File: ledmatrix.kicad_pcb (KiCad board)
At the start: 2 copper layers, 75.6 x 37.8 mm, 27 parts, among them J1 BUS_IN1, J2 BUS_IN2, J3 BUS_OUT1, J4 BUS_OUT2, Q1 PMV50XP, Q2 PMV50XP, Q3 PMV50XP, Q4 PMV50XP, Q5 PMV50XP, Q6 PMV50XP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

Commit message: fix matrix module order
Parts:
- Q7, R9: moved to B.Cu
- moved Q7 45.1 mm to (37.9, 38.4), turned to 180 degrees
- moved R9 44.9 mm to (38.4, 35.6), turned to 180 degrees
- moved U1 37.8 mm to (82.1, 44.3)
- moved U3 37.8 mm to (44.3, 44.3)
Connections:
- U2 pad 13: /matrix_1/COL_EN -> /GND
- U4 pad 13: /matrix_1/COL_EN -> /GND
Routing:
- net /CDO: track 0.00 -> 100.0 mm
- net /matrix_2/COL_DI: track 0.00 -> 40.3 mm, vias 0 -> 4
- net Net-(U3-Pad3): track 22.4 -> 0.00 mm, vias 1 -> 0
- net Net-(U3-Pad4): track 22.2 -> 0.00 mm, vias 1 -> 0
- net /Row Control/RC7: track 0.00 -> 21.9 mm, vias 0 -> 1
- net /CLE: track 61.6 -> 83.1 mm
- net Net-(U3-Pad11): track 16.5 -> 0.00 mm, vias 1 -> 0
- net Net-(U3-Pad6): track 11.9 -> 0.00 mm
- net /ROW_7: track 38.8 -> 41.1 mm
- net Net-(Q7-Pad1): track 0.00 -> 1.92 mm

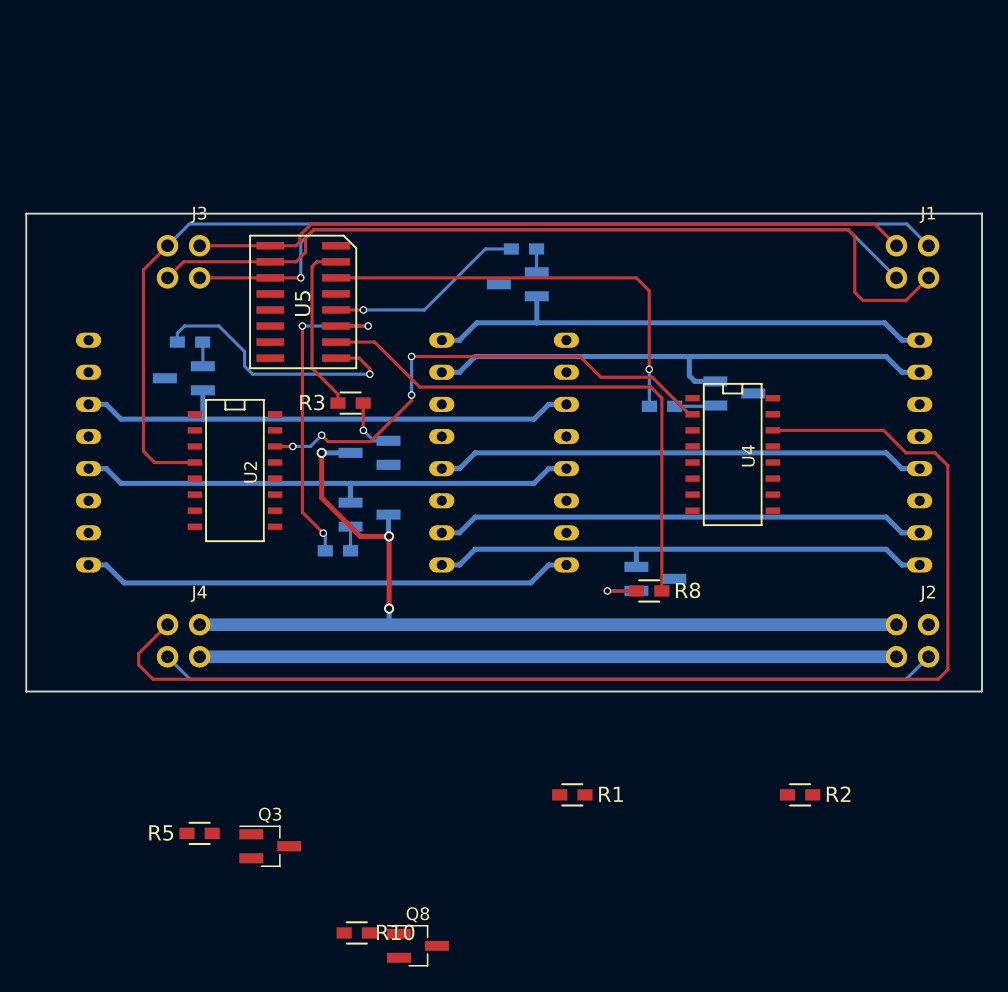
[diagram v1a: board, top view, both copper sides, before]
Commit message: cleaner vcc, gnd on left side
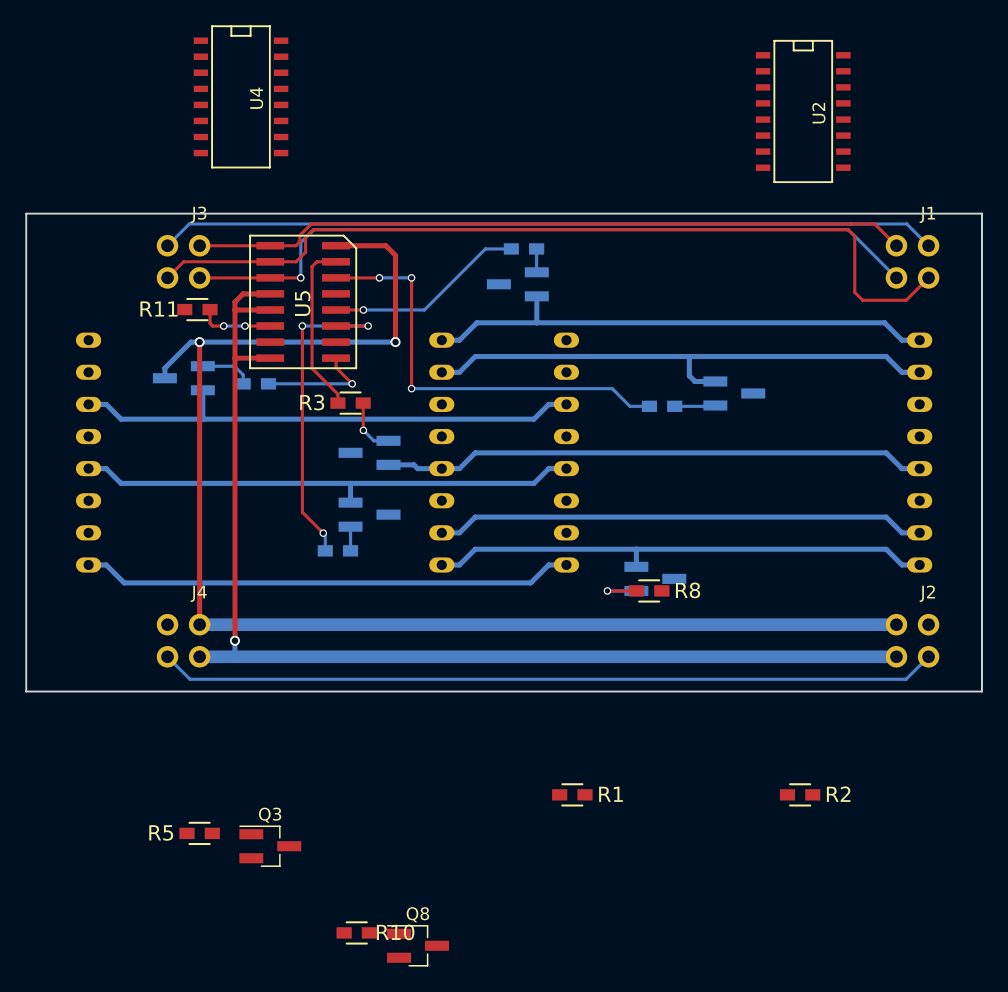
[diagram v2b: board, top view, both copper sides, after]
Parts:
- added R11: 10k, footprints:0603_HAND, F.Cu at (38.9, 33.0)
- moved U2 53.2 mm to (86.9, 17.3)
- moved U4 48.1 mm to (42.4, 16.2)
- moved R9 6.17 mm to (43.6, 38.9), turned to 0 degrees
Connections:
- U5 pad 6: (no net) -> /REN
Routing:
- net /CDO: track 100.0 -> 0.00 mm
- net /Row Control/RC6: track 42.9 -> 0.00 mm
- net /matrix_2/COL_DI: track 40.3 -> 0.00 mm, vias 4 -> 0
- net /GND: track 55.1 -> 91.8 mm, vias 0 -> 1
- net /VCC: track 76.3 -> 109.2 mm, vias 3 -> 2
- net /CLE: track 83.1 -> 61.6 mm
- net /Row Control/RC7: track 21.9 -> 9.18 mm
- net /REN: track 0.00 -> 5.95 mm, vias 0 -> 2
- net /ROW_1: track 39.7 -> 44.0 mm
- net Net-(Q7-Pad1): track 1.92 -> 4.18 mm
- net /Row Control/RC2: track 34.3 -> 34.1 mm, vias 1 -> 3

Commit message: finish left side traces
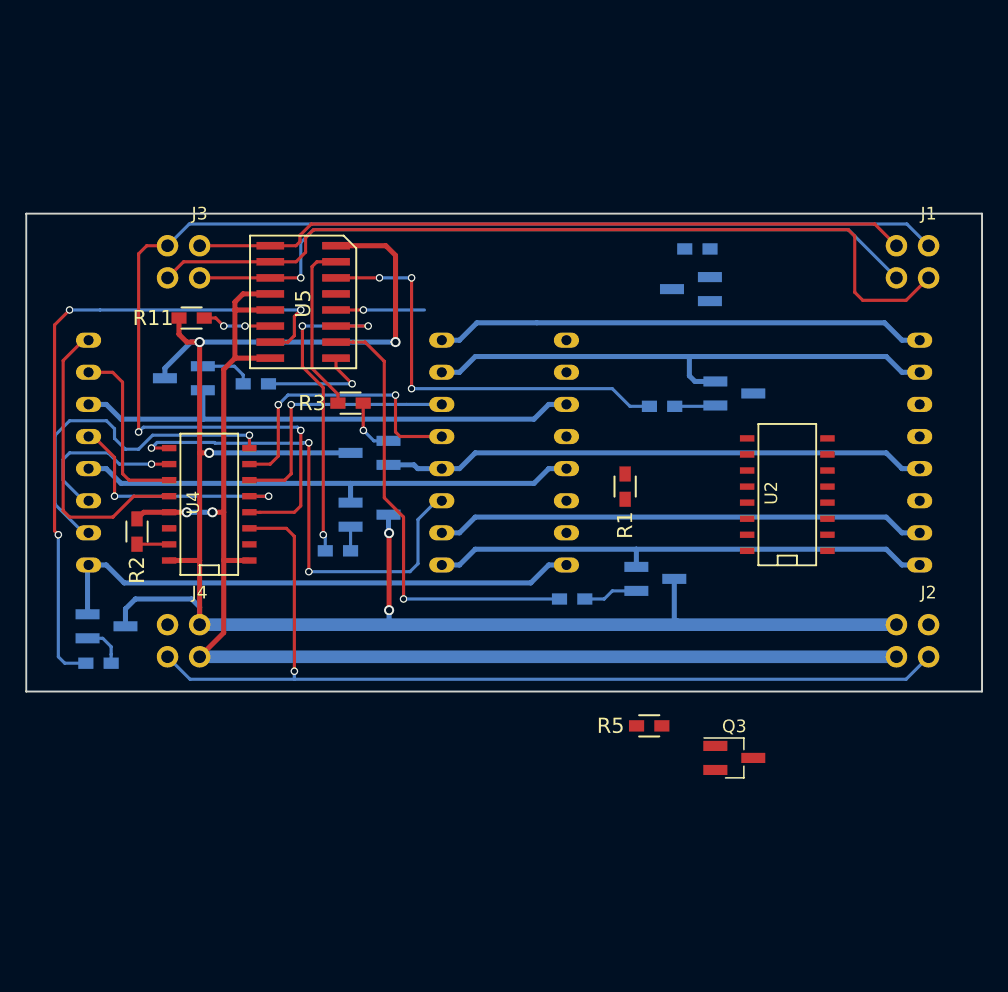
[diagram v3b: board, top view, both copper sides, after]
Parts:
- Q8, R10, R8: moved to B.Cu
- moved R2 56.4 mm to (34.2, 50.5), turned to 270 degrees
- moved Q3 37.4 mm to (81.4, 68.5)
- moved R5 36.6 mm to (74.7, 65.9)
- moved Q8 35.3 mm to (31.8, 58.0)
- moved U4 32.3 mm to (39.9, 48.4), turned to 90 degrees
- moved U2 30.3 mm to (85.6, 47.6), turned to 90 degrees
- moved R10 29.5 mm to (31.1, 61.0), turned to 180 degrees
- moved R1 24.7 mm to (72.8, 47.0), turned to 270 degrees
- moved R6 13.7 mm to (78.5, 28.2)
- moved Q4 13.7 mm to (78.0, 31.4)
- moved R8 6.13 mm to (68.6, 55.9), turned to 180 degrees
- moved R11 0.81 mm to (38.5, 33.7)
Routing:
- net /Row Control/RC8: track 0.00 -> 53.1 mm, vias 0 -> 3
- net /CLE: track 61.6 -> 101.6 mm, vias 0 -> 2
- net Net-(U3-Pad6): track 0.00 -> 39.9 mm, vias 0 -> 3
- net /VCC: track 109.2 -> 148.4 mm, vias 2 -> 5
- net /Row Control/RC6: track 0.00 -> 36.2 mm, vias 0 -> 1
- net Net-(U3-Pad10): track 0.00 -> 28.2 mm, vias 0 -> 1
- net Net-(U3-Pad16): track 0.00 -> 23.8 mm
- net Net-(U3-Pad4): track 0.00 -> 23.3 mm, vias 0 -> 2
- net Net-(U3-Pad3): track 0.00 -> 21.2 mm, vias 0 -> 1
- net Net-(U3-Pad13): track 0.00 -> 20.2 mm, vias 0 -> 2
- net /CCK: track 61.7 -> 76.8 mm, vias 0 -> 1
- net Net-(U3-Pad15): track 0.00 -> 14.5 mm
- net Net-(U3-Pad11): track 0.00 -> 13.4 mm, vias 0 -> 1
- net /GND: track 91.8 -> 102.1 mm, vias 1 -> 2
- net /Row Control/RC4: track 15.9 -> 6.99 mm
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
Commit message: add bypassing to schematic
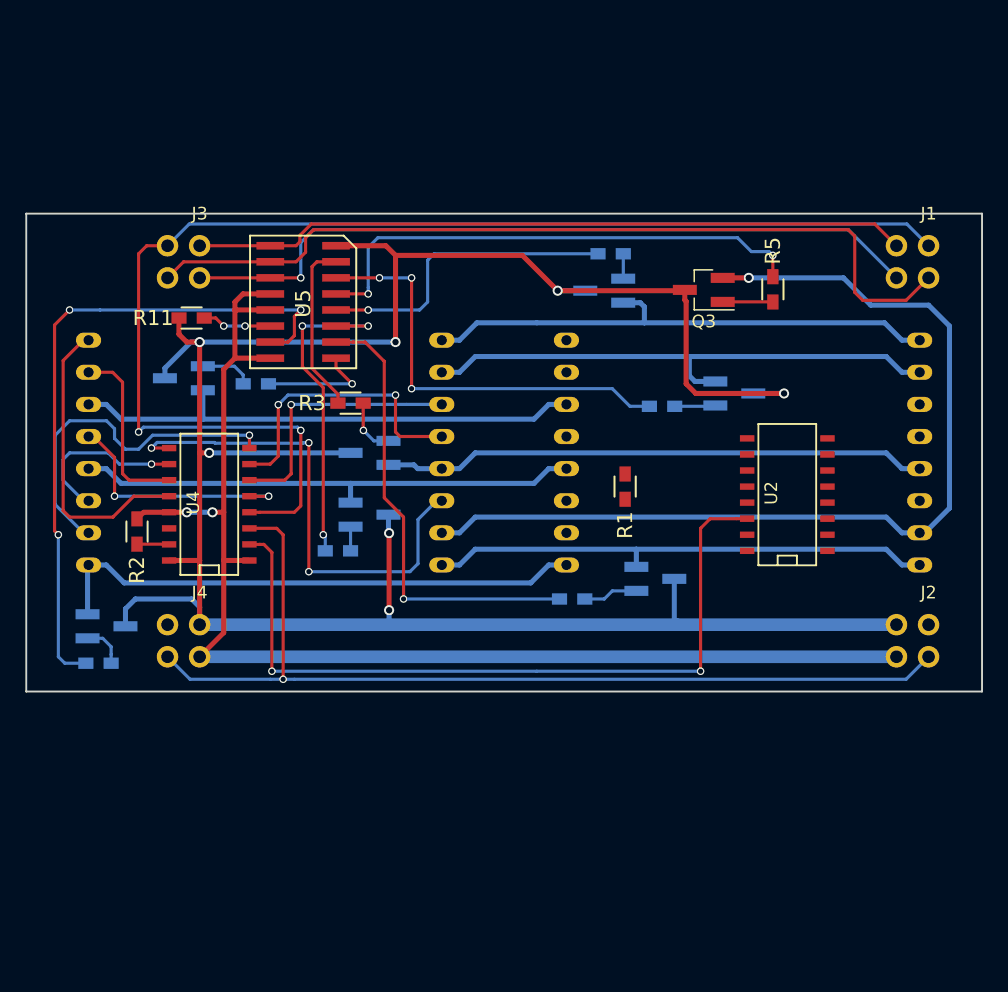
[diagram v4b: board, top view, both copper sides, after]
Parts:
- moved Q3 37.1 mm to (79.0, 31.4), turned to 180 degrees
- moved R5 35.9 mm to (84.5, 31.4), turned to 90 degrees
- moved R6 6.87 mm to (71.6, 28.6)
- moved Q4 6.86 mm to (71.1, 31.5)
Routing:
- net /matrix_2/COL_DI: track 0.00 -> 60.6 mm, vias 0 -> 2
- net /VCC: track 148.4 -> 192.6 mm, vias 5 -> 7
- net /Row Control/RC3: track 0.00 -> 40.8 mm, vias 0 -> 2
- net /ROW_3: track 38.8 -> 75.9 mm, vias 0 -> 1
- net /Row Control/RC4: track 6.99 -> 24.5 mm
- net Net-(Q3-Pad1): track 0.00 -> 3.96 mm
- net /ROW_4: track 39.3 -> 42.4 mm
- net Net-(Q4-Pad1): track 0.00 -> 1.97 mm

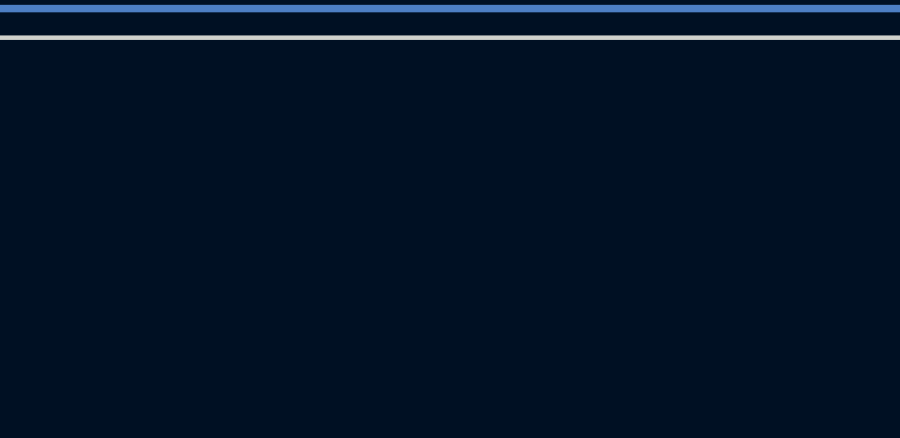
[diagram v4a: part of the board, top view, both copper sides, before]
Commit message: read bypassing netlist into pcbnew
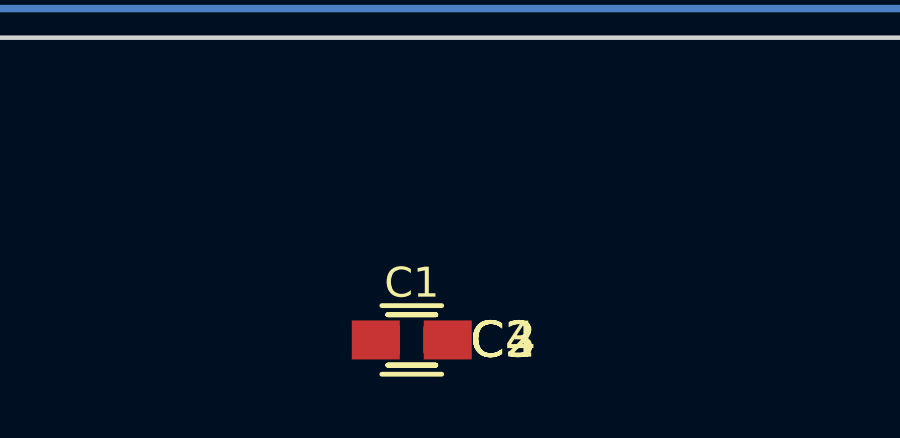
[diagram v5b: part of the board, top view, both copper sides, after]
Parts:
- added C1: 10u, footprints:0805_HAND, F.Cu at (63.2, 73.3)
- added C2, C3, C4: 1u, footprints:0603_HAND, F.Cu at (63.2, 73.3)
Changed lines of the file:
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@@
 (kicad_pcb (version 4) (host pcbnew 4.0.6)
   (general
-    (links 89)
-    (no_connects 27)
-    (area 25.024999 24.325 106.999001 72.128)
+    (links 96)
+    (no_connects 21)
+    (area 25.324999 25.324999 101.075001 63.275001)
     (thickness 1.6)
     (drawings 4)
     (tracks 394)
     (zones 0)
-    (modules 28)
+    (modules 32)
     (nets 54)
   )
@@
       (net 1 /VCC))
   )
+  (module footprints:0805_HAND (layer F.Cu)
+    (at 63.2 73.275001)
+    (fp_text reference C1 (at 0 -1.905) (layer F.SilkS)
+      (effects (font (size 1 1) (thickness 0.16)))
+    )
+    (fp_text value 10u (at 0 2.032) (layer F.Fab)
+      (effects (font (size 1 1) (thickness 0.16)))
+    )
+    (fp_line (start -1 1.143) (end 1 1.143) (layer F.SilkS) (width 0.16))
+    (fp_line (start -1 -1.143) (end 1 -1.143) (layer F.SilkS) (width 0.16))
+    (pad 1 smd rect (at -1.2 0) (size 1.6 1.3) (layers F.Cu F.Paste F.Mask))
+    (pad 2 smd rect (at 1.2 0) (size 1.6 1.3) (layers F.Cu F.Paste F.Mask)
+      (net 2 /GND))
+  )
+  (module footprints:0603_HAND (layer F.Cu)
+    (at 63.2 73.275001)
+    (fp_text reference C2 (at 3.048 0) (layer F.SilkS)
+      (effects (font (size 1.2 1.2) (thickness 0.2)))
+    )
+    (fp_text value 1u (at 0 1.651) (layer F.Fab)
+      (effects (font (size 1.2 1.2) (thickness 0.2)))
+    )
+    (fp_line (start -0.8 0.84) (end 0.8 0.84) (layer F.SilkS) (width 0.16))
+    (fp_line (start -0.8 -0.84) (end 0.8 -0.84) (layer F.SilkS) (width 0.16))
+    (pad 1 smd rect (at -1 0) (size 1.2 0.9) (layers F.Cu F.Paste F.Mask)
+      (net 1 /VCC))
+    (pad 2 smd rect (at 1 0) (size 1.2 0.9) (layers F.Cu F.Paste F.Mask)
+      (net 2 /GND))
+  )
+  (module footprints:0603_HAND (layer F.Cu)
+    (at 63.2 73.275001)
+    (fp_text reference C3 (at 3.048 0) (layer F.SilkS)
+      (effects (font (size 1.2 1.2) (thickness 0.2)))
+    )
+    (fp_text value 1u (at 0 1.651) (layer F.Fab)
+      (effects (font (size 1.2 1.2) (thickness 0.2)))
+    )
+    (fp_line (start -0.8 0.84) (end 0.8 0.84) (layer F.SilkS) (width 0.16))
+    (fp_line (start -0.8 -0.84) (end 0.8 -0.84) (layer F.SilkS) (width 0.16))
+    (pad 1 smd rect (at -1 0) (size 1.2 0.9) (layers F.Cu F.Paste F.Mask)
+      (net 1 /VCC))
+    (pad 2 smd rect (at 1 0) (size 1.2 0.9) (layers F.Cu F.Paste F.Mask)
+      (net 2 /GND))
+  )
+  (module footprints:0603_HAND (layer F.Cu)
+    (at 63.2 73.275001)
+    (fp_text reference C4 (at 3.048 0) (layer F.SilkS)
+      (effects (font (size 1.2 1.2) (thickness 0.2)))
+    )
+    (fp_text value 1u (at 0 1.651) (layer F.Fab)
+      (effects (font (size 1.2 1.2) (thickness 0.2)))
+    )
+    (fp_line (start -0.8 0.84) (end 0.8 0.84) (layer F.SilkS) (width 0.16))
+    (fp_line (start -0.8 -0.84) (end 0.8 -0.84) (layer F.SilkS) (width 0.16))
+    (pad 1 smd rect (at -1 0) (size 1.2 0.9) (layers F.Cu F.Paste F.Mask)
+      (net 2 /GND))
+    (pad 2 smd rect (at 1 0) (size 1.2 0.9) (layers F.Cu F.Paste F.Mask)
+      (net 1 /VCC))
+  )

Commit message: fully connected PCB
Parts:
- C1: moved to B.Cu
- moved C4 46.1 mm to (54.7, 27.9), turned to 180 degrees
- moved C3 29.7 mm to (40.0, 54.7)
- moved C2 29.3 mm to (85.6, 54.4)
- moved C1 24.7 mm to (42.9, 59.2), turned to 270 degrees
- moved R1 8.80 mm to (80.1, 51.8), turned to 90 degrees
- moved R9 0.72 mm to (43.1, 39.4)
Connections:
- C1 pad 1: (no net) -> /VCC
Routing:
- net /GND: track 102.1 -> 189.6 mm, vias 2 -> 7
- net /CLE: track 101.6 -> 133.3 mm
- net Net-(U1-Pad13): track 0.00 -> 31.6 mm, vias 0 -> 1
- net Net-(U1-Pad10): track 0.00 -> 28.4 mm, vias 0 -> 2
- net Net-(U1-Pad16): track 0.00 -> 23.3 mm
- net Net-(U1-Pad15): track 0.00 -> 22.3 mm, vias 0 -> 2
- net /CCK: track 76.3 -> 97.2 mm
- net /VCC: track 192.6 -> 210.4 mm, vias 7 -> 11
- net Net-(U1-Pad6): track 0.00 -> 17.6 mm, vias 0 -> 1
- net /CDO: track 0.00 -> 17.4 mm, vias 0 -> 2
- net Net-(U1-Pad11): track 0.00 -> 17.0 mm, vias 0 -> 1
- net /CDI: track 0.00 -> 14.3 mm
- net Net-(U1-Pad4): track 0.00 -> 12.6 mm, vias 0 -> 1
- net Net-(U1-Pad3): track 0.00 -> 11.9 mm
- net /Row Control/RC8: track 53.1 -> 48.2 mm
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
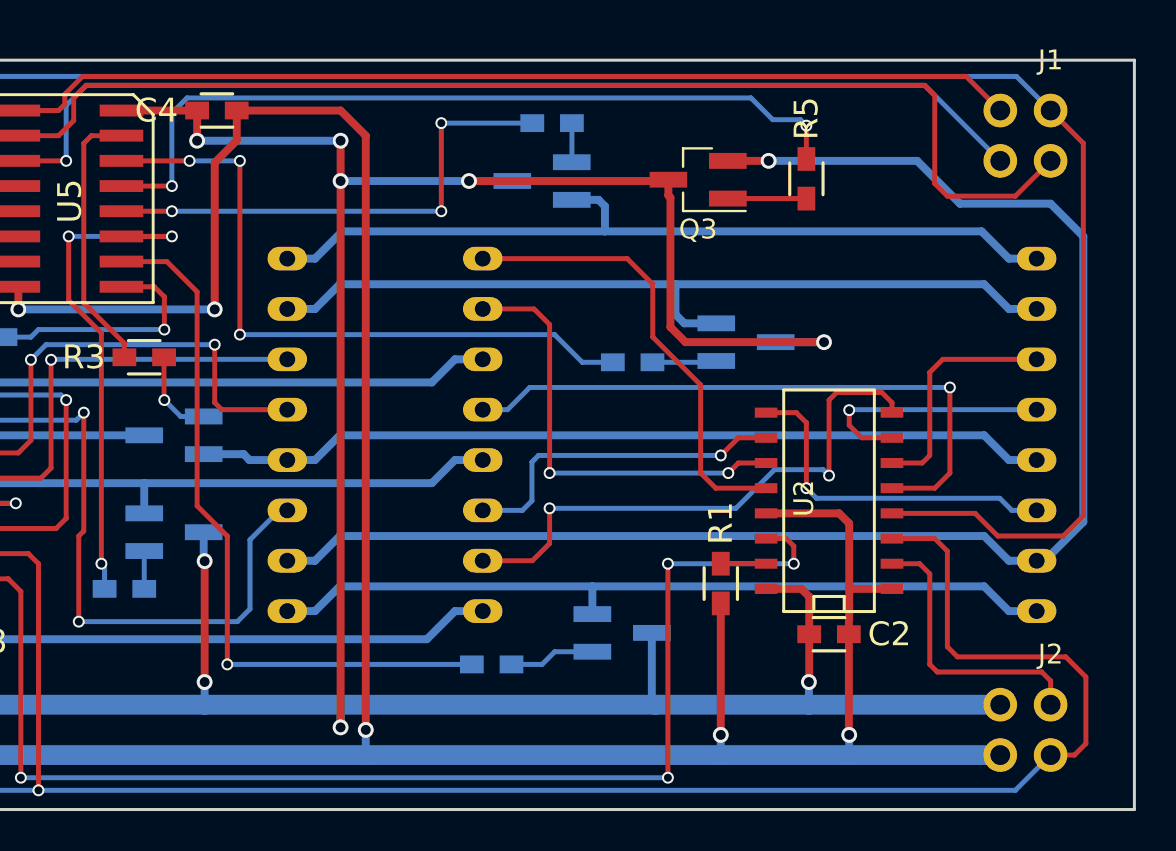
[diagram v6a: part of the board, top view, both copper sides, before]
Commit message: move R3 driver closer to R3
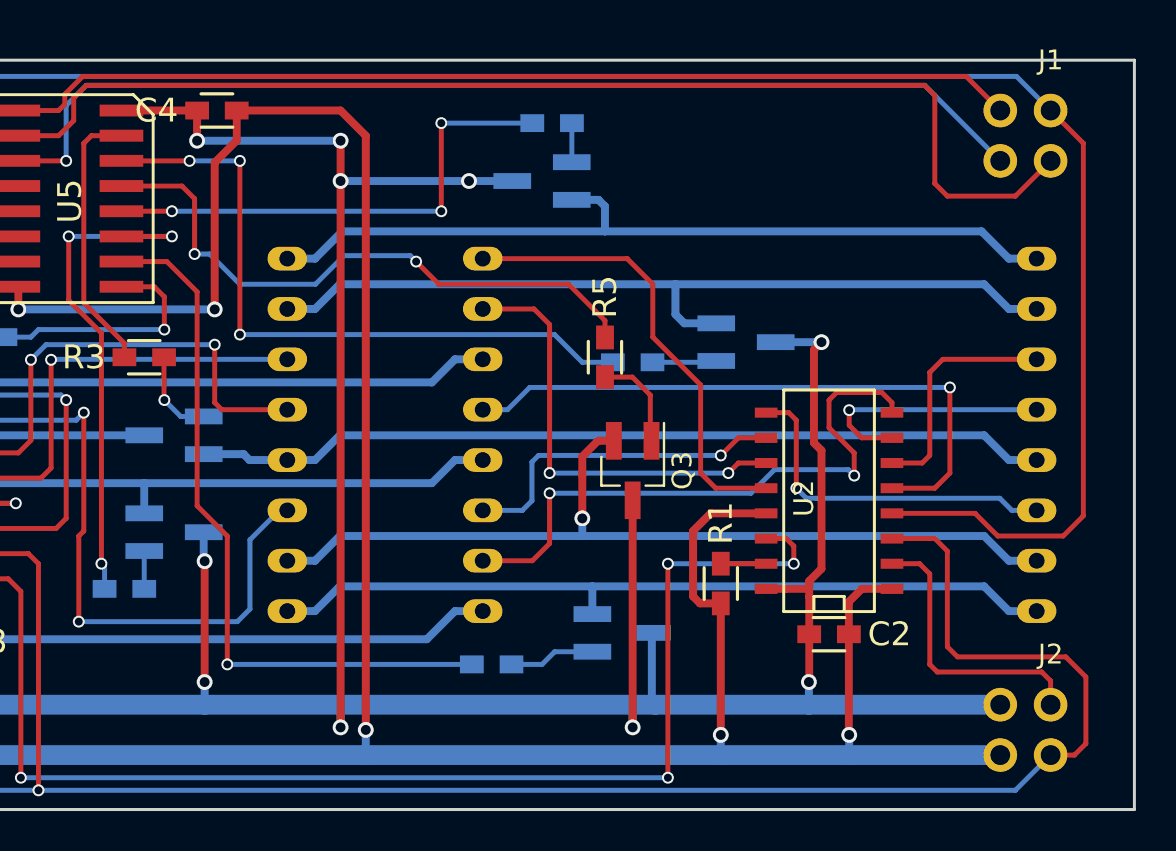
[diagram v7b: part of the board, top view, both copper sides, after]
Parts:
- moved Q3 15.0 mm to (75.7, 46.1), turned to 270 degrees
- moved R5 13.6 mm to (74.3, 40.4)
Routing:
- net /ROW_3: track 75.9 -> 45.2 mm
- net /Row Control/RC3: track 40.8 -> 30.9 mm
- net Net-(U1-Pad10): track 28.4 -> 30.6 mm
- net Net-(Q3-Pad1): track 3.96 -> 5.00 mm
- net /GND: track 189.6 -> 190.4 mm
- net /VCC: track 210.4 -> 210.5 mm, vias 11 -> 12
